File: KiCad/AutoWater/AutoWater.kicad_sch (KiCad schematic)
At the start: 0 parts

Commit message: Create electric schema
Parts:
- added BT1: DS-201, symbol AutoWater:Power raw DS-201
- added BT2: Battery_Cell, symbol Device:Battery_Cell
- added C1, C2: Capacitor, symbol AutoWater:Capacitor
- added C3: 100nF, symbol AutoWater:Capacitor
- added D1, D2, D3, D4, D5, D6, D7, D8: LED, symbol AutoWater:LED
- added IC1: 74ABT125PW, symbol AutoWater:74ABT125PW
- added LCD1: LCD I2C module, symbol AutoWater:LCD I2C module
- added MCU1: Arduino Nano, symbol AutoWater:Arduino Nano V3 Type C
- added P1: Pump, symbol AutoWater:Pump
- added Q1: Transistor NPN, symbol AutoWater:Transistor NPN
- added R1, R15, R16, R17, R2, R3, R4, R5, R6, R7, R8, R9: Resistor, symbol AutoWater:Resistor
- added R10, R11, R12, R13: 3.3K, symbol AutoWater:Resistor
- added R14: 10K, symbol AutoWater:Resistor
- added REG1: 74HC164, symbol AutoWater:Shift register
- added RTC1: DS1307, symbol AutoWater:RTC DS1307
- added RV1, RV2: Sensor, symbol AutoWater:Moisture sensor module
- added SD1: Micro SD connector, symbol AutoWater:MicroSD
- added STB1: 5V, symbol AutoWater:Stabalizer voltage
- added SW1, SW2: Button, symbol AutoWater:Button
- added Y1: Crystal, symbol Device:Crystal
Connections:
- new net: R3.1, REG1.Q6
- new net: D2.VCC, R3.2
- new net: R6.1, REG1.Q3
- new net: D5.VCC, R6.2
- new net: LCD1.SCL, MCU1.A5 (SCL), R15.2, RTC1.SCL
- new net: MCU1.D11 (MOSI), R10.1
- new net: IC1.2, R10.2
- new net: MCU1.A0 (Sensor_0), RV1.A
- new net: IC1.8, SD1.2 (CMD)
- new net: IC1.3, SD1.3 (VSS1)
- new net: IC1.6, SD1.5 (CLK)
- new net: R13.2, SD1.7 (DAT0)
- new net: IC1.9, R12.2
- new net: R8.1, REG1.Q1
- new net: D7.VCC, R8.2
- new net: D8.VCC, R9.2
- new net: LCD1.SDA, MCU1.A4 (SDA), R16.2, RTC1.SDA
- new net: MCU1.D13 (SCK), R11.1
- new net: IC1.5, R11.2
- new net: R2.1, REG1.Q7
- new net: D1.VCC, R2.2
- new net: Q1.B, R1.2
- new net: P1.GND, Q1.C
- new net: MCU1.D7 (RtcConfirm), SW1.2
- new net: BT2.1 (+), RTC1.Vbat
- new net: IC1.13, MCU1.D10 (SdCs), R12.1, R14.2
- new net: R17.2, RTC1.SQW/OUT
- new net: RTC1.X1, Y1.2
- new net: RTC1.X2, Y1.1
- new net: MCU1.D2 (Pump), R1.1
- new net: MCU1.D4 (StateClk), REG1.CP
- new net: MCU1.D3 (StateSer), REG1.DSB
- new net: R9.1, REG1.Q0
- new net: R7.1, REG1.Q2
- new net: R5.1, REG1.Q4
- new net: R4.1, REG1.Q5
- new net: D6.VCC, R7.2
- new net: MCU1.RL (RST), SW2.2
- new net: D4.VCC, R5.2
- new net: MCU1.A1 (Sensor_1), RV2.A
- new net: IC1.11, MCU1.D12 (MISO)
- new net: IC1.12, R13.1
- new net: D3.VCC, R4.2
- new net +3V3: C3.VCC, IC1.14 (VCC), MCU1.3V3, R14.1, SD1.4 (VDD)
- new net +5V: C2.VCC, LCD1.VCC, P1.VCC, R15.1, R16.1, R17.1, REG1.DSA, REG1.MR, REG1.VCC, RTC1.Vcc, STB1.Vout
- new net GND: BT1.2 (-), BT2.2 (-), C1.GND, C2.GND, C3.GND, D1.GND, D2.GND, D3.GND, D4.GND, D5.GND, D6.GND, D7.GND, D8.GND, IC1.1, IC1.10, IC1.4, IC1.7 (GND), LCD1.GND, MCU1.GL (GND), Q1.E, REG1.GND, RTC1.GND, RV1.GND, RV2.GND, SD1.6 (VSS2), STB1.GND, SW1.1, SW2.1
- new net VCC RAW: BT1.1 (+), C1.VCC, MCU1.VIN, STB1.Vin
- new net VCC sensors: MCU1.D9 (SensorsPower), RV1.VCC, RV2.VCC
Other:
- title: (none) -> AutoWater

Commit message: Add nominals
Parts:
- BT2: value Battery_Cell -> CR2032
- C1, C2: value Capacitor -> 10 mkF
- R2, R3, R4, R5, R6, R7, R8, R9: value Resistor -> 150R
- Y1: value Crystal -> 32.768kHz
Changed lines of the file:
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@@
 		(dnp no)
 		(property "Reference" "R3"
-			(at 130.81 73.66 0)
+			(at 130.81 71.755 0)
 			(do_not_autoplace yes)
 			(effects
@@
 			)
 		)
-		(property "Value" "Resistor"
+		(property "Value" "150R"
 			(at 130.81 73.66 0)
 			(effects
@@
 					(size 1.27 1.27)
 				)
-				(hide yes)
 			)
 		)
@@
 		(dnp no)
 		(property "Reference" "R6"
-			(at 130.81 88.9 0)
+			(at 130.81 86.995 0)
 			(do_not_autoplace yes)
 			(effects
@@
 			)
 		)
-		(property "Value" "Resistor"
+		(property "Value" "150R"
 			(at 130.81 88.9 0)
 			(effects
@@
 					(size 1.27 1.27)
 				)
-				(hide yes)
 			)
 		)
@@
 		(dnp no)
 		(property "Reference" "R8"
-			(at 130.81 99.06 0)
+			(at 130.81 97.155 0)
 			(do_not_autoplace yes)
 			(effects
@@
 			)
 		)
-		(property "Value" "Resistor"
+		(property "Value" "150R"
 			(at 130.81 99.06 0)
 			(effects
@@
 					(size 1.27 1.27)
 				)
-				(hide yes)
 			)
 		)
@@
 		(dnp no)
 		(property "Reference" "R2"
-			(at 130.81 68.58 0)
+			(at 130.81 66.675 0)
 			(do_not_autoplace yes)
 			(effects
@@
 			)
 		)
-		(property "Value" "Resistor"
+		(property "Value" "150R"
 			(at 130.81 68.58 0)
 			(effects
@@
 					(size 1.27 1.27)
 				)
-				(hide yes)
 			)
 		)
@@
 			)
 		)
-		(property "Value" "Capacitor"
+		(property "Value" "10 mkF"
 			(at 33.655 48.26 0)
 			(effects
@@
 				)
 				(justify left)
-				(hide yes)
 			)
 		)
@@
 			)
 		)
-		(property "Value" "Battery_Cell"
-			(at 267.335 37.465 0)
+		(property "Value" "CR2032"
+			(at 271.78 37.465 0)
 			(effects
 				(font
@@
 			)
 		)
-		(property "Value" "Capacitor"
+		(property "Value" "10 mkF"
 			(at 48.895 48.26 0)
 			(effects
@@
 				)
 				(justify left)
-				(hide yes)
 			)
 		)
@@
 		(dnp no)
 		(property "Reference" "R5"
-			(at 130.81 83.82 0)
+			(at 130.81 81.915 0)
 			(do_not_autoplace yes)
 			(effects
@@
 			)
 		)
-		(property "Value" "Resistor"
+		(property "Value" "150R"
 			(at 130.81 83.82 0)
 			(effects
@@
 					(size 1.27 1.27)
 				)
-				(hide yes)
 			)
 		)
@@
 			)
 		)
-		(property "Value" "Crystal"
+		(property "Value" "32.768kHz"
 			(at 272.415 48.26 90)
 			(effects
@@
 		(dnp no)
 		(property "Reference" "R9"
-			(at 130.81 104.14 0)
+			(at 130.81 102.235 0)
 			(do_not_autoplace yes)
 			(effects
@@
 			)
 		)
-		(property "Value" "Resistor"
+		(property "Value" "150R"
 			(at 130.81 104.14 0)
 			(effects
@@
 					(size 1.27 1.27)
 				)
-				(hide yes)
 			)
 		)
@@
 		(dnp no)
 		(property "Reference" "R4"
-			(at 130.81 78.74 0)
+			(at 130.81 76.835 0)
 			(do_not_autoplace yes)
 			(effects
@@
 			)
 		)
-		(property "Value" "Resistor"
+		(property "Value" "150R"
 			(at 130.81 78.74 0)
 			(effects
@@
 					(size 1.27 1.27)
 				)
-				(hide yes)
 			)
 		)
@@
 		(dnp no)
 		(property "Reference" "R7"
-			(at 130.81 93.98 0)
+			(at 130.81 92.075 0)
 			(do_not_autoplace yes)
 			(effects
@@
 			)
 		)
-		(property "Value" "Resistor"
+		(property "Value" "150R"
 			(at 130.81 93.98 0)
 			(effects
@@
 					(size 1.27 1.27)
 				)
-				(hide yes)
 			)
 		)

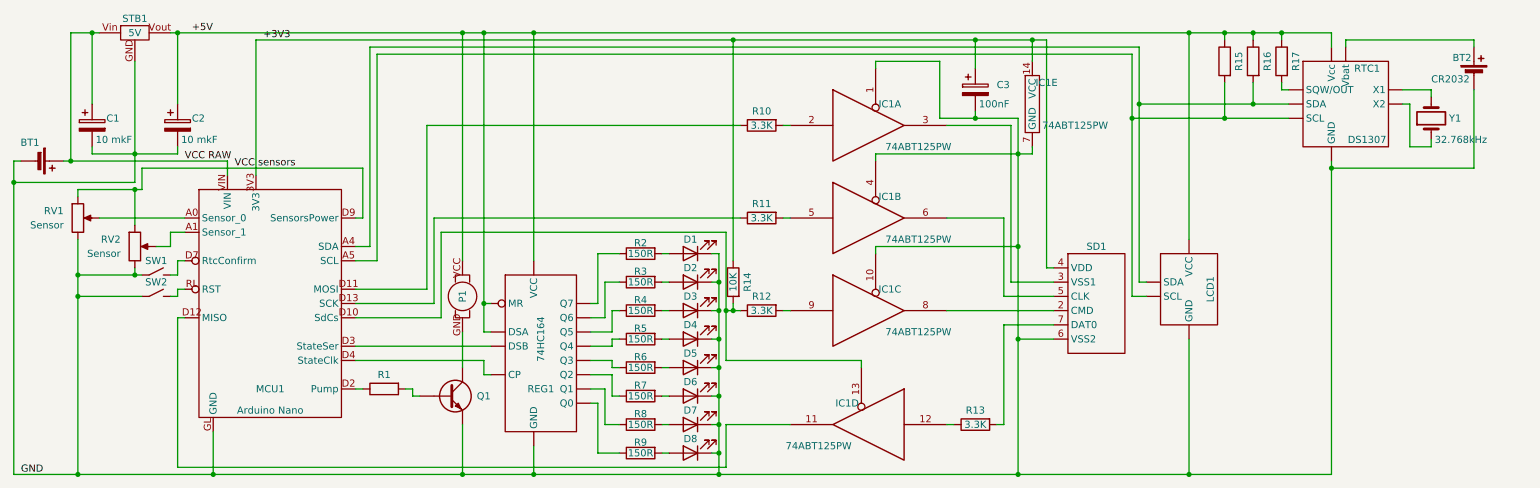
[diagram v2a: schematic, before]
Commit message: Replace I2C resisters
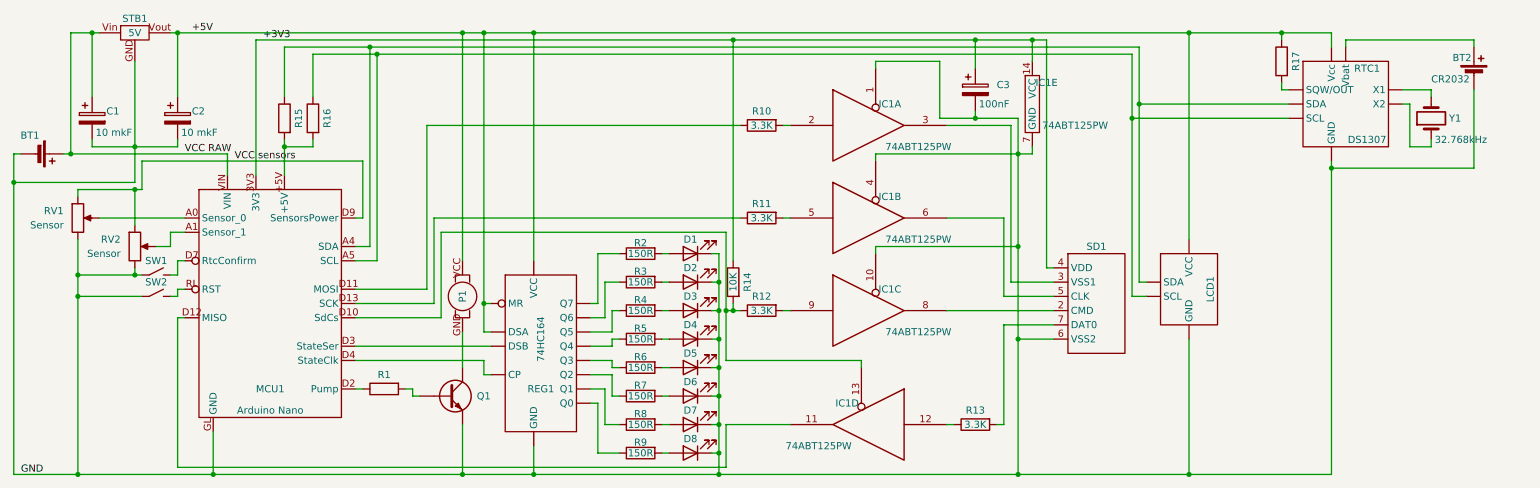
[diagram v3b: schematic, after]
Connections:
- net +5V: no longer R15.1, R16.1
- net at LCD1.SCL, MCU1.A5 (SCL), RTC1.SCL: now also R16.1; no longer R15.2
- net at LCD1.SDA, MCU1.A4 (SDA), RTC1.SDA: now also R15.1; no longer R16.2
- new net: MCU1.+5V, R15.2, R16.2
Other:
- moved on the sheet: BT1, C1, C2, R15, R16

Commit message: Create layout placed
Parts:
- added C4: 0.1mkF, AutoWater:Capacity SMD 0603, symbol AutoWater:Capacitor
- added D9: S1BFL, AutoWater:Diode S1BFL, symbol Device:D
- BT1: footprint (none) -> AutoWater:Connector 5.5x2.1 DS-201
- BT2: footprint (none) -> AutoWater:Batary box CR2032
- C1, C2, C3: footprint (none) -> AutoWater:Capacity SMD 0603
- D1, D2, D3, D4, D5, D6, D7, D8: footprint (none) -> AutoWater:LED 3mm
- IC1: footprint (none) -> AutoWater:Buffers TSSOP-14
- LCD1: footprint (none) -> AutoWater:PLS-4
- MCU1: footprint (none) -> AutoWater:Arduino Nano V3 Type C PBS
- P1, SW1, SW2: footprint (none) -> AutoWater:Connector B2B-XH-A
- Q1: footprint (none) -> AutoWater:NPN transistor BC817-25
- R1: renamed from R15; value Resistor -> 2.2K; footprint (none) -> AutoWater:Resistor 0805
- R10: renamed from R8; footprint (none) -> AutoWater:Resistor 0805
- R11: renamed from R9; footprint (none) -> AutoWater:Resistor 0805
- R12: renamed from R14; footprint (none) -> AutoWater:Resistor 0805
- R13: renamed from R10; footprint (none) -> AutoWater:Resistor 0805
- R14: renamed from R11; footprint (none) -> AutoWater:Resistor 0805
- R15: renamed from R12; footprint (none) -> AutoWater:Resistor 0805
- R16: renamed from R13; footprint (none) -> AutoWater:Resistor 0805
- R17: value Resistor -> 2.2K; footprint (none) -> AutoWater:Resistor 0805
- R2: renamed from R16; value Resistor -> 2.2K; footprint (none) -> AutoWater:Resistor 0805
- R3: renamed from R1; value Resistor -> 2,2K; footprint (none) -> AutoWater:Resistor 0805
- R4: renamed from R2; footprint (none) -> AutoWater:Resistor 0805
- R5: renamed from R3; footprint (none) -> AutoWater:Resistor 0805
- R6: renamed from R4; footprint (none) -> AutoWater:Resistor 0805
- R7: renamed from R5; footprint (none) -> AutoWater:Resistor 0805
- R8: renamed from R6; footprint (none) -> AutoWater:Resistor 0805
- R9: renamed from R7; footprint (none) -> AutoWater:Resistor 0805
- REG1: footprint (none) -> AutoWater:Register 74HC164M SOP-14
- RTC1: footprint (none) -> AutoWater:RTC DS1307 DIP
- RV1, RV2: footprint (none) -> AutoWater:PLS-3
- SD1: footprint (none) -> AutoWater:MicroSD
- STB1: footprint (none) -> AutoWater:Stabilizer 5V AMS1117-5.0S SMD
- Y1: footprint (none) -> AutoWater:Crystal 32768 SMD
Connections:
- net +5V: now also C4.VCC, D9.1 (K)
- net at P1.GND, Q1.C: now also C4.GND, D9.2 (A)
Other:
- moved on the sheet: BT2, C3, D1, D2, D3, D4, D5, D6, D7, D8, IC1A, IC1B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
